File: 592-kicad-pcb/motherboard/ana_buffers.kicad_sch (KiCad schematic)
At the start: 7 parts, among them J2 U.FL, J3 U.FL, J4 2.54mm 1x2, J5 2.54mm 1x1, U4 OPA2328DR, U5 74LVC1T45GW

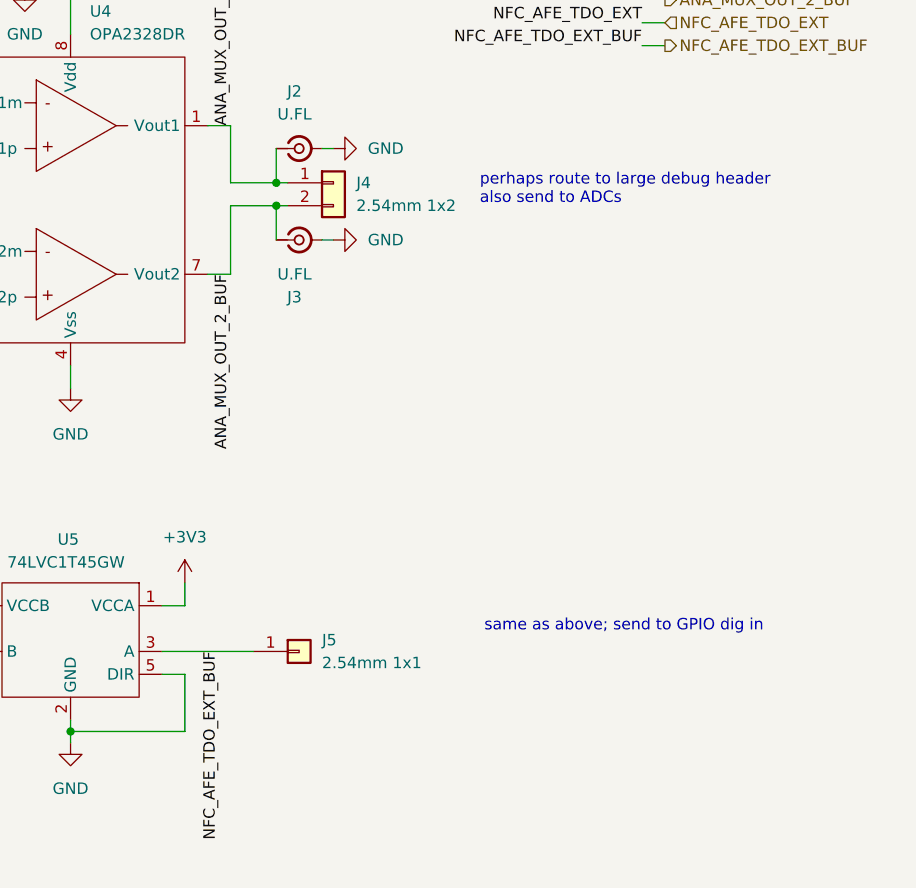
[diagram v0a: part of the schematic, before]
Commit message: clean up supporting blocks; add nucleo symbol
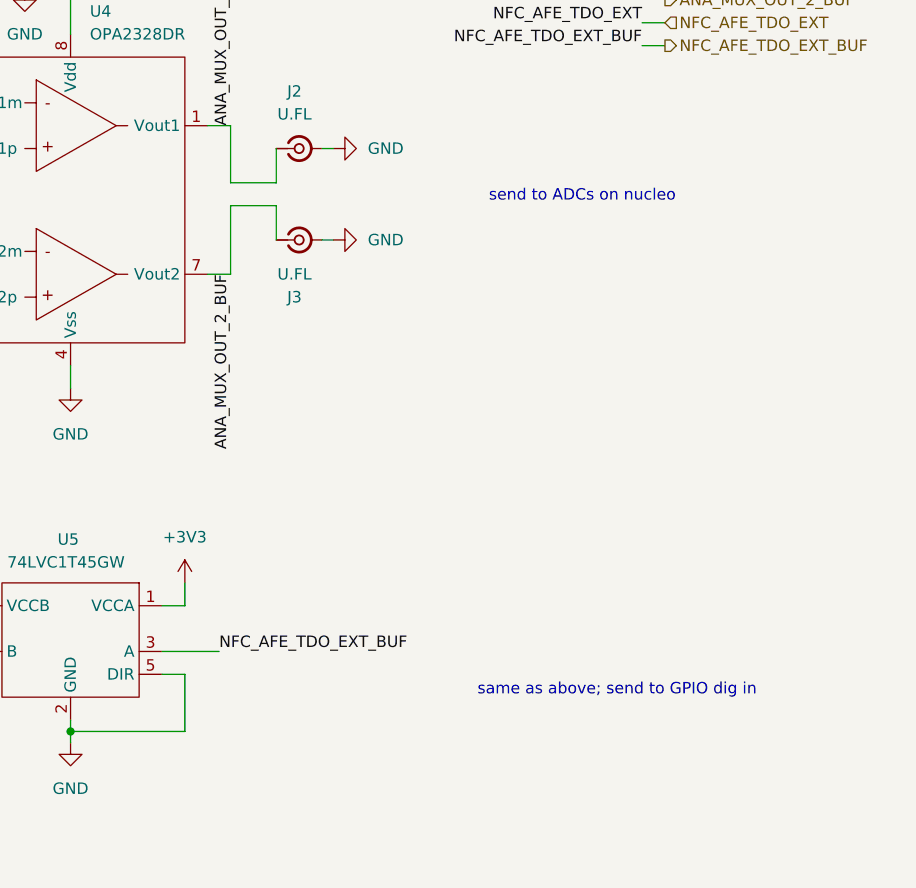
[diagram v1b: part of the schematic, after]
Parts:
- removed J4: 2.54mm 1x2, symbol Connector_Generic:Conn_01x02
- removed J5: 2.54mm 1x1, symbol Connector_Generic:Conn_01x01
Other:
- note added: "send to ADCs on nucleo"
- note removed: "perhaps route to large debug header also send to ADCs"
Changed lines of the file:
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@@
 		(company "john kesler (jckesle2@ncsu.edu)")
 	)
-	(text "perhaps route to large debug header\nalso send to ADCs"
+	(text "send to ADCs on nucleo"
 		(exclude_from_sim no)
-		(at 115.316 62.992 0)
+		(at 116.332 63.754 0)
 		(effects
 			(font
@@
 	(text "same as above; send to GPIO dig in"
 		(exclude_from_sim no)
-		(at 115.824 111.506 0)
+		(at 115.062 118.618 0)
 		(effects
 			(font
@@
 		(color 0 0 0 0)
 	)
-	(junction
-		(at 92.71 62.23)
-		(diameter 0)
-		(color 0 0 0 0)
-	)
-	(junction
-		(at 92.71 64.77)
-		(diameter 0)
-		(color 0 0 0 0)
-	)
 	(wire
 		(pts
@@
 	(wire
 		(pts
-			(xy 80.01 114.3) (xy 90.17 114.3)
-		)
-		(stroke
-			(width 0)
-			(type default)
-		)
-	)
-	(wire
-		(pts
 			(xy 85.09 72.39) (xy 87.63 72.39)
 		)
@@
 	(wire
 		(pts
+			(xy 80.01 114.3) (xy 86.36 114.3)
+		)
+		(stroke
+			(width 0)
+			(type default)
+		)
+	)
+	(wire
+		(pts
 			(xy 80.01 116.84) (xy 82.55 116.84)
 		)
@@
 	(wire
 		(pts
-			(xy 92.71 62.23) (xy 93.98 62.23)
-		)
-		(stroke
-			(width 0)
-			(type default)
-		)
-	)
-	(wire
-		(pts
 			(xy 97.79 68.58) (xy 99.06 68.58)
 		)
@@
 		(pts
 			(xy 133.35 44.45) (xy 135.89 44.45)
-		)
-		(stroke
-			(width 0)
-			(type default)
-		)
-	)
-	(wire
-		(pts
-			(xy 92.71 64.77) (xy 93.98 64.77)
 		)
 		(stroke
@@
 	)
 	(label "NFC_AFE_TDO_EXT_BUF"
-		(at 86.36 114.3 270)
-		(effects
-			(font
-				(size 1.27 1.27)
-			)
-			(justify right bottom)
+		(at 86.36 114.3 0)
+		(effects
+			(font
+				(size 1.27 1.27)
+			)
+			(justify left bottom)
 		)
 	)
@@
 				(path "/5b0c97ac-fa03-4db8-b41b-0eee32b6f55d/9cc7bda2-6b63-4506-9986-d8a2a58c5915"
 					(reference "#PWR019")
-					(unit 1)
-				)
-			)
-		)
-	)
-	(symbol
-		(lib_id "Connector_Generic:Conn_01x02")
-		(at 99.06 62.23 0)
-		(unit 1)
-		(exclude_from_sim no)
-		(in_bom yes)
-		(on_board yes)
-		(dnp no)
-		(fields_autoplaced yes)
-		(property "Reference" "J4"
-			(at 101.6 62.2299 0)
-			(effects
-				(font
-					(size 1.27 1.27)
-				)
-				(justify left)
-			)
-		)
-		(property "Value" "2.54mm 1x2"
-			(at 101.6 64.7699 0)
-			(effects
-				(font
-					(size 1.27 1.27)
-				)
-				(justify left)
-			)
-		)
-		(property "Footprint" ""
-			(at 99.06 62.23 0)
-			(effects
-				(font
-					(size 1.27 1.27)
-				)
-				(hide yes)
-			)
-		)
-		(property "Datasheet" "~"
-			(at 99.06 62.23 0)
-			(effects
-				(font
-					(size 1.27 1.27)
-				)
-				(hide yes)
-			)
-		)
-		(property "Description" "Generic connector, single row, 01x02, script generated (kicad-library-utils/schlib/autogen/connector/)"
-			(at 99.06 62.23 0)
-			(effects
-				(font
-					(size 1.27 1.27)
-				)
-				(hide yes)
-			)
-		)
-		(pin "1"
-		)
-		(pin "2"
-		)
-		(instances
-			(project ""
-				(path "/5b0c97ac-fa03-4db8-b41b-0eee32b6f55d/9cc7bda2-6b63-4506-9986-d8a2a58c5915"
-					(reference "J4")
 					(unit 1)
 				)
@@
 			)
 		)
-		(property "Datasheet" ""
+		(property "Datasheet" "https://www.lcsc.com/datasheet/C478004.pdf"
 			(at 69.85 113.03 0)
 			(effects
@@
 			)
 		)
-		(property "Datasheet" ""
+		(property "Datasheet" "https://www.lcsc.com/datasheet/C5214797.pdf"
 			(at 69.85 64.77 0)
 			(effects
@@
 					(unit 1)
 				)
-			)
-		)
-	)
-	(symbol
-		(lib_id "Connector_Generic:Conn_01x01")
-		(at 95.25 114.3 0)
-		(unit 1)
-		(exclude_from_sim no)
-		(in_bom yes)
-		(on_board yes)
-		(dnp no)
-		(fields_autoplaced yes)
-		(property "Reference" "J5"
-			(at 97.79 113.0299 0)
-			(effects
-				(font
-					(size 1.27 1.27)
-				)
-				(justify left)
-			)
-		)
-		(property "Value" "2.54mm 1x1"
-			(at 97.79 115.5699 0)
-			(effects
-				(font
-					(size 1.27 1.27)
-				)
-				(justify left)
-			)
-		)
-		(property "Footprint" ""
-			(at 95.25 114.3 0)
-			(effects
-				(font
-					(size 1.27 1.27)
-				)
-				(hide yes)
-			)
-		)
-		(property "Datasheet" "~"
-			(at 95.25 114.3 0)
-			(effects
-				(font
-					(size 1.27 1.27)
-				)
-				(hide yes)
-			)
-		)
-		(property "Description" "Generic connector, single row, 01x01, script generated (kicad-library-utils/schlib/autogen/connector/)"
-			(at 95.25 114.3 0)
-			(effects
-				(font
-					(size 1.27 1.27)
-				)
-				(hide yes)
-			)
-		)
-		(pin "1"
-		)
-		(instances
-			(project ""
-				(path "/5b0c97ac-fa03-4db8-b41b-0eee32b6f55d/9cc7bda2-6b63-4506-9986-d8a2a58c5915"
-					(reference "J5")
-					(unit 1)
-				)

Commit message: add footprints for signal conditioning
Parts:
- C2: footprint (none) -> Capacitor_SMD:C_0603_1608Metric
- J2, J3: footprint (none) -> Connector_Coaxial:U.FL_Hirose_U.FL-R-SMT-1_Vertical
- U4: footprint (none) -> Package_SO:VSSOP-8_3x3mm_P0.65mm
- U5: footprint (none) -> Package_TO_SOT_SMD:SOT-363_SC-70-6
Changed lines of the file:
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@@
 			)
 		)
-		(property "Footprint" ""
+		(property "Footprint" "Connector_Coaxial:U.FL_Hirose_U.FL-R-SMT-1_Vertical"
 			(at 95.25 58.42 0)
 			(effects
@@
 			)
 		)
-		(property "Footprint" ""
+		(property "Footprint" "Package_TO_SOT_SMD:SOT-363_SC-70-6"
 			(at 69.85 113.03 0)
 			(effects
@@
 			)
 		)
-		(property "Footprint" ""
+		(property "Footprint" "Package_SO:VSSOP-8_3x3mm_P0.65mm"
 			(at 69.85 64.77 0)
 			(effects
@@
 			)
 		)
-		(property "Footprint" ""
+		(property "Footprint" "Connector_Coaxial:U.FL_Hirose_U.FL-R-SMT-1_Vertical"
 			(at 95.25 68.58 0)
 			(effects
@@
 			)
 		)
-		(property "Footprint" ""
+		(property "Footprint" "Capacitor_SMD:C_0603_1608Metric"
 			(at 64.77 35.56 0)
 			(effects

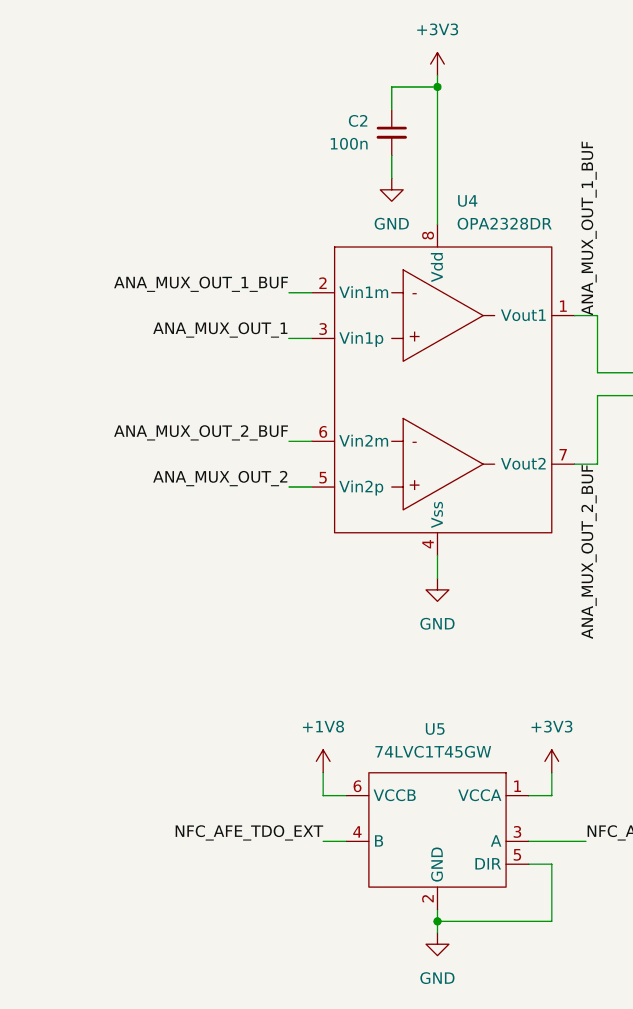
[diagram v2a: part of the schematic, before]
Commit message: update motheboard schems to include conn
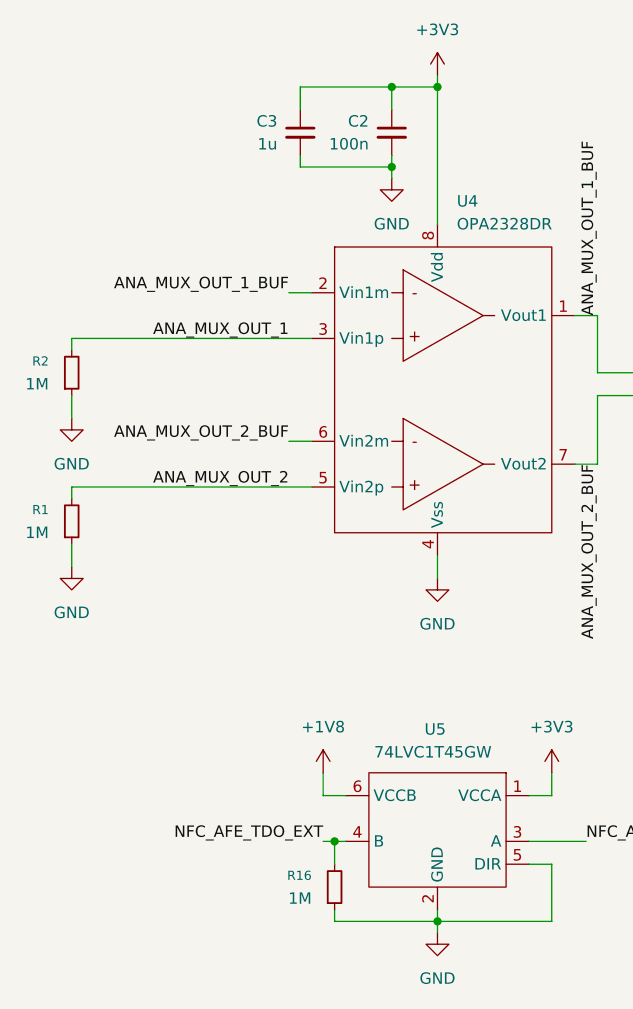
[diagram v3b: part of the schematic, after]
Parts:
- added C3: 1u, Capacitor_SMD:C_0603_1608Metric, symbol Device:C_Small
- added R1, R16, R2: 1M, symbol Device:R_Small
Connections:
- net +3V3: now also C3.1
- net ANA_MUX_OUT_1: now also R2.2
- net ANA_MUX_OUT_2: now also R1.2
- net GND: now also C3.2, R1.1, R16.1, R2.1
- net NFC_AFE_TDO_EXT: now also R16.2

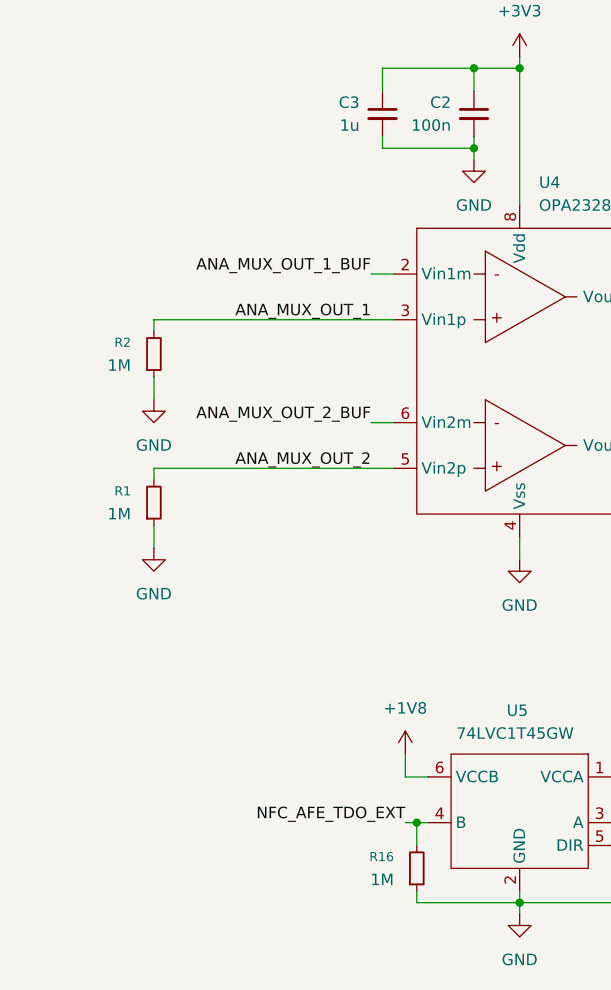
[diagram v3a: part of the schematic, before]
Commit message: clean up some pull up/downs
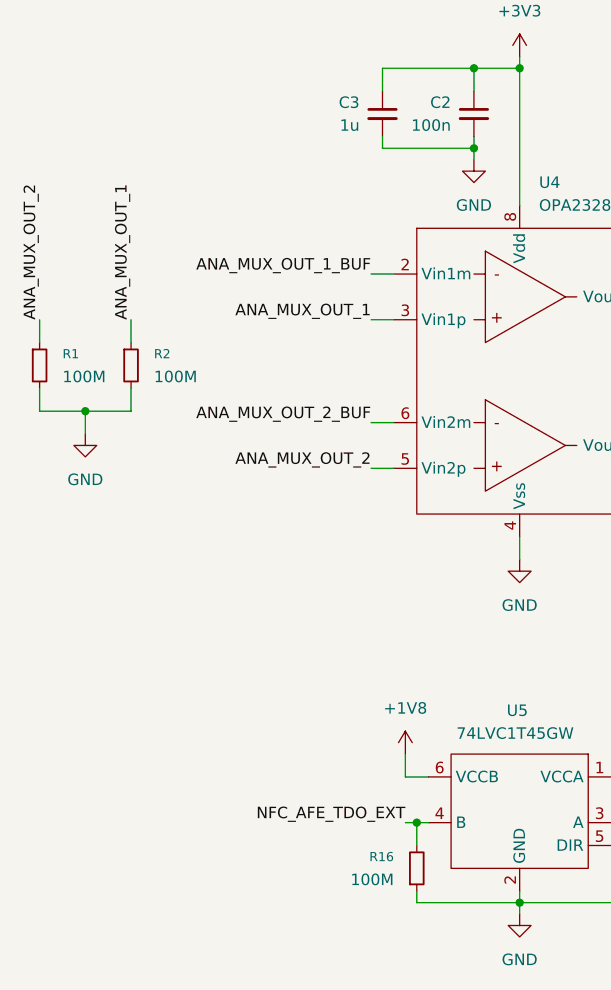
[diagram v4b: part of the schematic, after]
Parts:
- R1, R16, R2: value 1M -> 100M
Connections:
- net ANA_MUX_OUT_1: now also R2.1; no longer R2.2
- net ANA_MUX_OUT_2: now also R1.1; no longer R1.2
- net GND: now also R1.2, R2.2; no longer R1.1, R2.1

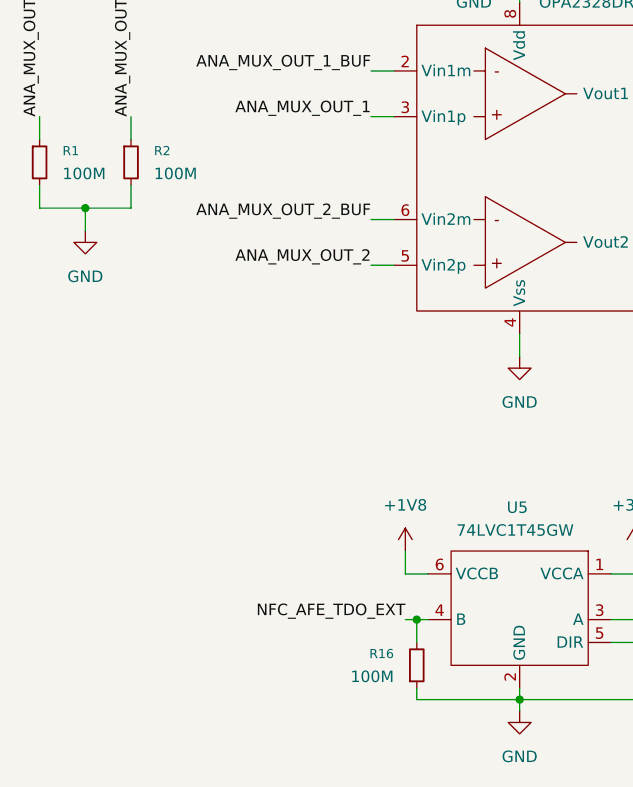
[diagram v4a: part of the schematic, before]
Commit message: add jlc stackup, size pulldowns
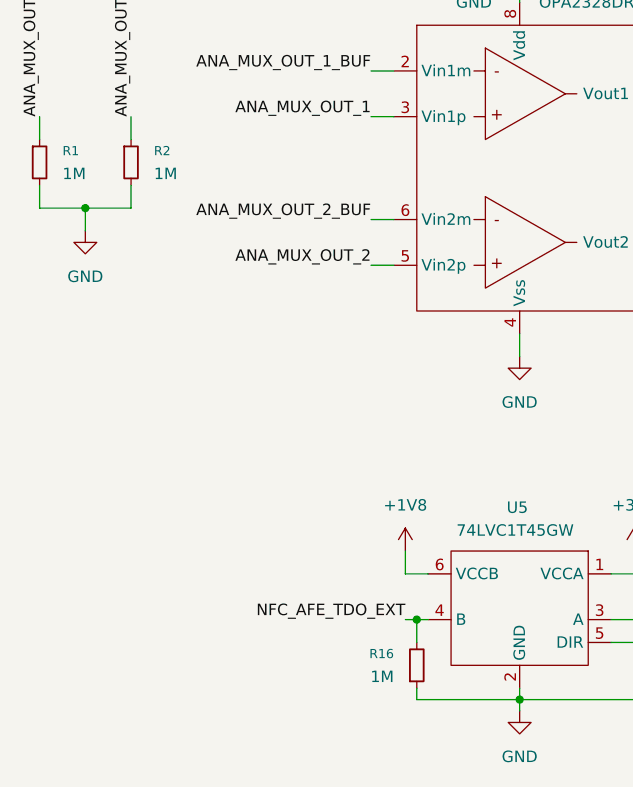
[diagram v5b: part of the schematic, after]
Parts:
- R1, R16, R2: value 100M -> 1M; footprint (none) -> Resistor_SMD:R_0603_1608Metric
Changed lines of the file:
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@@
 			)
 		)
-		(property "Value" "100M"
+		(property "Value" "1M"
 			(at 29.21 64.7699 0)
 			(effects
@@
 			)
 		)
-		(property "Footprint" ""
+		(property "Footprint" "Resistor_SMD:R_0603_1608Metric"
 			(at 26.67 63.5 0)
 			(effects
@@
 			)
 		)
-		(property "Value" "100M"
+		(property "Value" "1M"
 			(at 19.05 64.7699 0)
 			(effects
@@
 			)
 		)
-		(property "Footprint" ""
+		(property "Footprint" "Resistor_SMD:R_0603_1608Metric"
 			(at 16.51 63.5 0)
 			(effects
@@
 			)
 		)
-		(property "Value" "100M"
+		(property "Value" "1M"
 			(at 55.88 120.6499 0)
 			(effects
@@
 			)
 		)
-		(property "Footprint" ""
+		(property "Footprint" "Resistor_SMD:R_0603_1608Metric"
 			(at 58.42 119.38 0)
 			(effects
